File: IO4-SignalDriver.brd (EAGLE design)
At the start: 99.8 x 80.5 mm, 21 parts, among them CON1 CONNECTOR-RJ45-FRONT, IC1 74LS139N, P1 500R, P2 500R, P3 500R, P4 500R, P5 500R, P6 500R

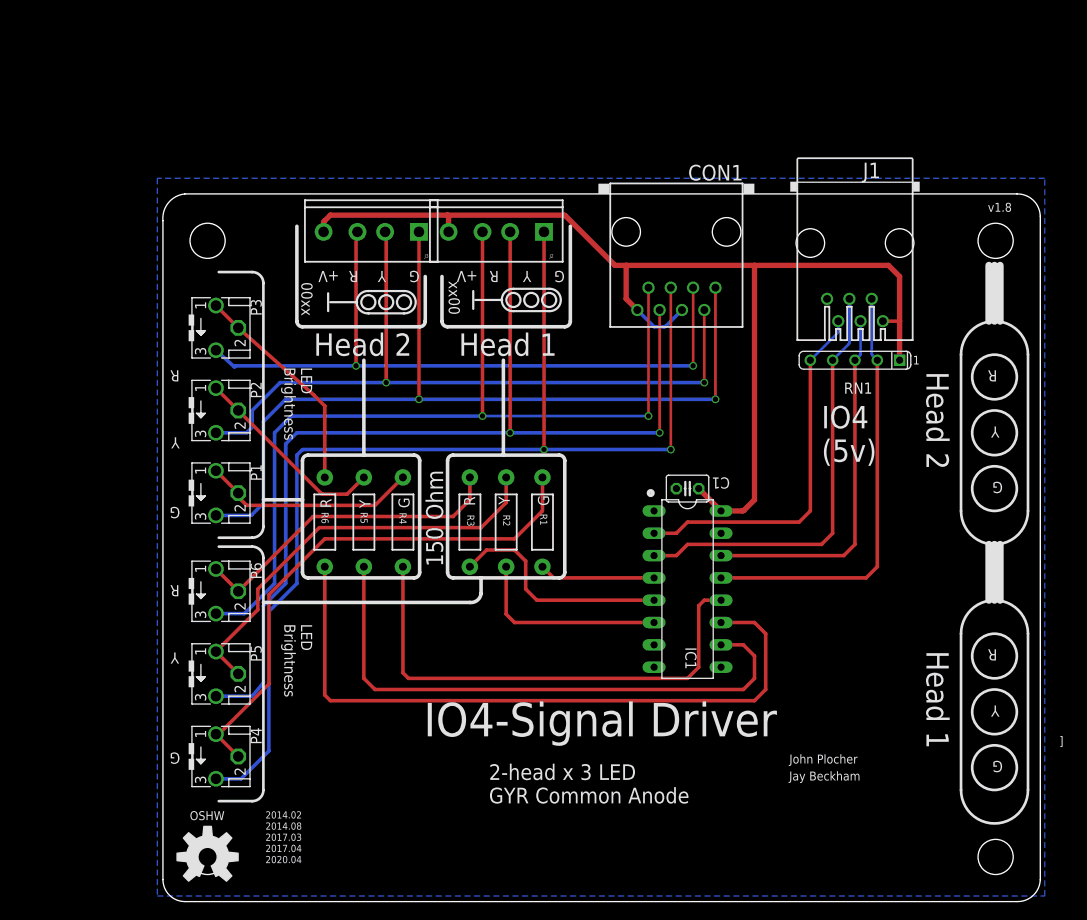
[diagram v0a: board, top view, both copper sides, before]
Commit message: convert to SMT, add 2mmx4 headers
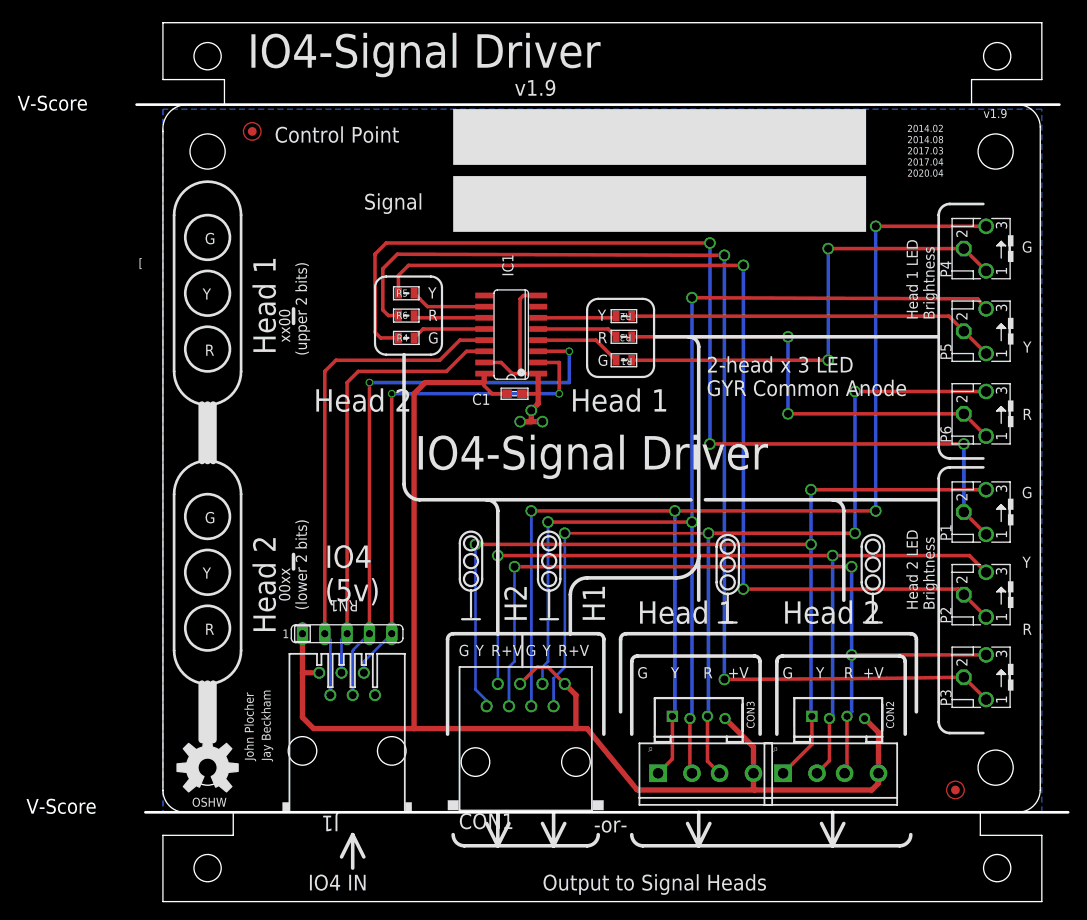
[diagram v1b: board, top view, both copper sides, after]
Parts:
- added CON2, CON3: CONNECTOR-GROVE-4P-2.0-3470130P1, SPCoast:4P-2.0
- added FID1, FID2: FIDUCIAL, SPCoast:FIDUCIAL_1MM
- BOARD1: value (none) -> BOARD80X100
- C1: device rcl:C025-030X050 -> SPCoast:0603-CAP
- CON1: value CONNECTOR-RJ45-FRONT -> (none)
- IC1: value 74LS139N -> 74LS139D; device 74xx-us:DIL16 -> SPCoast:SO16
- J1: device MCP:520250-3 -> SPCoast:RJ25-PANEL
- R1, R2, R3, R4, R5, R6: value 150R -> 470R; device SparkFun:AXIAL-0.4 -> SPCoast:0805-RES
- moved P4 104.4 mm to (93.3, 74.3), turned to 90 degrees
- moved P3 95.6 mm to (93.3, 25.5), turned to 90 degrees
- moved P5 95.3 mm to (93.3, 64.9), turned to 90 degrees
- moved P2 89.5 mm to (93.3, 34.9), turned to 90 degrees
- moved P6 89.3 mm to (93.3, 55.5), turned to 90 degrees
- moved P1 87.0 mm to (93.3, 44.3), turned to 90 degrees
- moved J1 81.7 mm to (21.0, 17.1), turned to 0 degrees
- moved J3 74.4 mm to (70.7, 14.6), turned to 0 degrees
- moved RN1 65.6 mm to (21.0, 30.5), turned to 0 degrees
- moved J2 63.0 mm to (56.5, 14.6), turned to 0 degrees
- moved CON1 62.7 mm to (41.3, 15.9), turned to 0 degrees
- moved IC1 35.2 mm to (39.6, 64.5), turned to 90 degrees
- moved R3 27.4 mm to (52.5, 64.3), turned to 180 degrees
- moved R2 27.0 mm to (52.5, 66.6), turned to 180 degrees
- moved R5 26.5 mm to (27.7, 69.2), turned to 0 degrees
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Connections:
- net G1: now also R4.2; no longer R4.P$2
- net G1-LED: now also CON2.1
- net G1V: now also R4.1; no longer R4.P$1
- net G2: now also R1.2; no longer R1.P$2
- net G2-LED: now also CON3.1
- net G2V: now also R1.1; no longer R1.P$1
- net R1: now also R6.2; no longer R6.P$2
- net R1-LED: now also CON2.3
- net R1V: now also R6.1; no longer R6.P$1
- net R2: now also R3.2; no longer R3.P$2
- net R2-LED: now also CON3.3
- net R2V: now also R3.1; no longer R3.P$1
- net VCC: now also CON2.4, CON3.4
- net Y1: now also R5.2; no longer R5.P$2
- net Y1-LED: now also CON2.2
- net Y1V: now also R5.1; no longer R5.P$1
- net Y2: now also R2.2; no longer R2.P$2
- net Y2-LED: now also CON3.2
- net Y2V: now also R2.1; no longer R2.P$1
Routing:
- net R1V: track 25.0 -> 125.4 mm, vias 0 -> 2
- net G1V: track 24.5 -> 113.5 mm, vias 0 -> 3
- net Y1V: track 22.6 -> 107.5 mm, vias 0 -> 2
- net R1: track 77.5 -> 8.07 mm
- net Y1: track 65.1 -> 8.60 mm
- net G1: track 56.3 -> 8.39 mm
- net VCC: track 130.1 -> 162.8 mm
- net GND: track 0.00 -> 31.1 mm, vias 0 -> 3
- net N$6: track 48.8 -> 66.2 mm, vias 0 -> 2
- net R2: track 26.0 -> 9.22 mm
- net N$5: track 41.7 -> 58.0 mm, vias 0 -> 2
- net R1-LED: track 79.2 -> 93.6 mm, vias 2 -> 3
- net Y2: track 22.6 -> 8.93 mm
- net R2V: track 36.8 -> 50.1 mm, vias 0 -> 2
- net Y1-LED: track 84.6 -> 96.5 mm
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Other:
- board size 99.8 x 80.5 mm -> 106 x 100 mm
- board text added: "-or-"
- board text added: "00xx (lower 2 bits)"
- board text added: "Changes: Silk Screen alignment, tweeking spaced fixed resistors further apart min trace width 16mil SMT components 2mmx4 headers"
- board text added: "Control Point"
- board text added: "H1"
- board text added: "H2"
- board text added: "Head 1 LED Brightness"
- board text added: "Head 2 LED Brightness"
- board text added: "IO4 IN"
- board text added: "Output to Signal Heads"
- board text added: "Signal"
- board text added: "v1.9"
- board text added: "xx00 (upper 2 bits)"
- board text removed: "00xx"
- board text removed: "150 Ohm"
- board text removed: "Changes: Silk Screen alignment, tweeking spaced fixed resistors further apart min trace width 16mil"
- board text removed: "LED Brightness"
- board text removed: "v1.8"
- board text removed: "xx00"

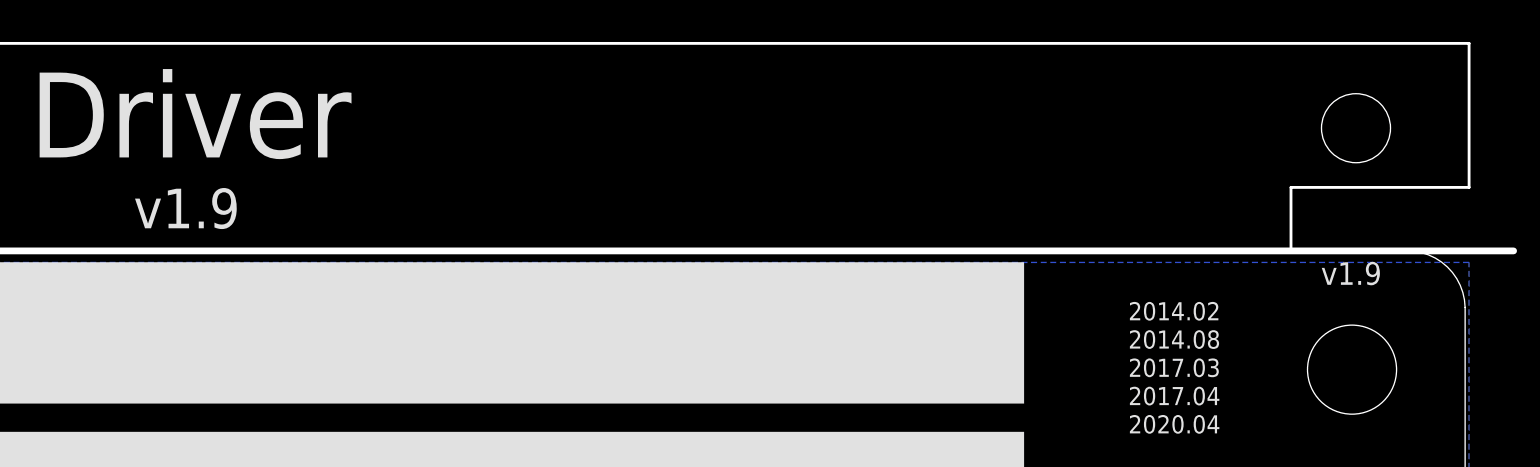
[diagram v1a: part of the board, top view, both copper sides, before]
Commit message: changed silkscreen version info
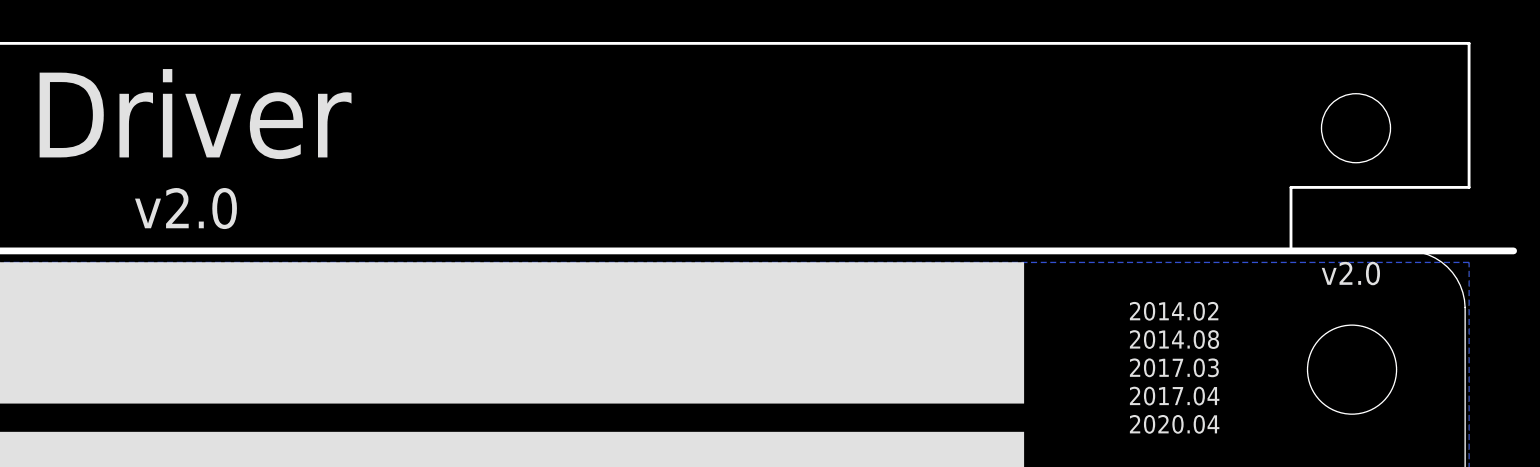
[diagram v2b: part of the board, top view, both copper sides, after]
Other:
- board text added: "v2.0"
- board text removed: "v1.9"
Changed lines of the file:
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@@
 <plain>
 <text x="28.653" y="49.157" size="3.81" layer="21" rot="SR0">IO4-Signal Driver</text>
-<text x="93.345" y="89.154" size="1.016" layer="21" rot="SR0">v1.9</text>
+<text x="93.345" y="89.154" size="1.016" layer="21" rot="SR0">v2.0</text>
 <text x="12.2555" y="16.002" size="1.016" layer="21" rot="SR90">Jay Beckham</text>
 <text x="10.327" y="16.028" size="1.016" layer="21" rot="SR90">John Plocher</text>
@@
 <text x="43.18" y="1.27" size="1.778" layer="21" font="vector" ratio="10">Output to Signal Heads</text>
 <text x="9.603" y="94.877" size="3.81" layer="21" rot="SR0">IO4-Signal Driver</text>
-<text x="40.005" y="91.694" size="1.778" layer="21" rot="SR0">v1.9</text>
+<text x="40.005" y="91.694" size="1.778" layer="21" rot="SR0">v2.0</text>
 <wire x1="38.1" y1="6.35" x2="39.37" y2="8.89" width="0.4064" layer="21"/>
 <wire x1="38.1" y1="6.35" x2="36.83" y2="8.89" width="0.4064" layer="21"/>

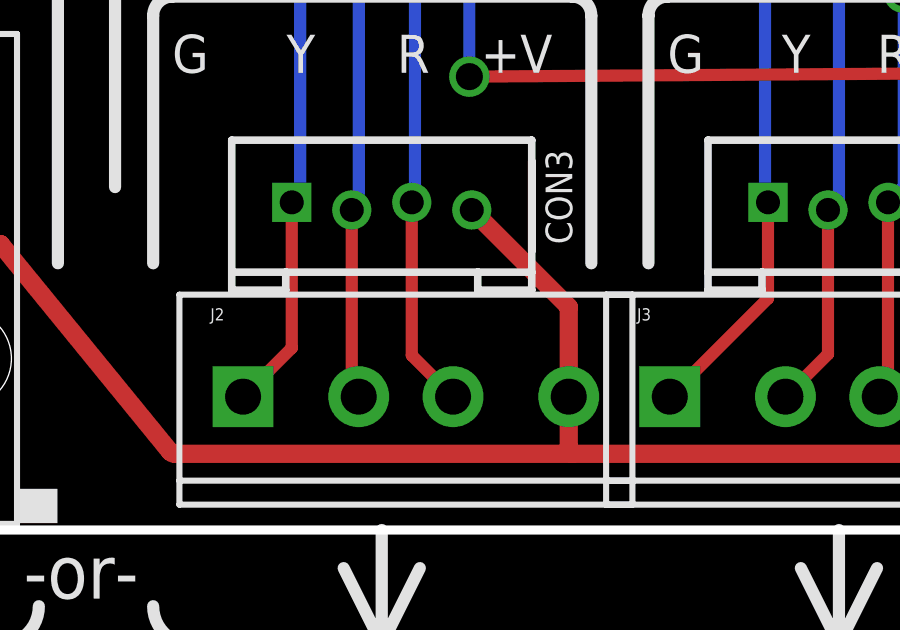
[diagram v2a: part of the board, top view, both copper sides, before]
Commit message: font=vector
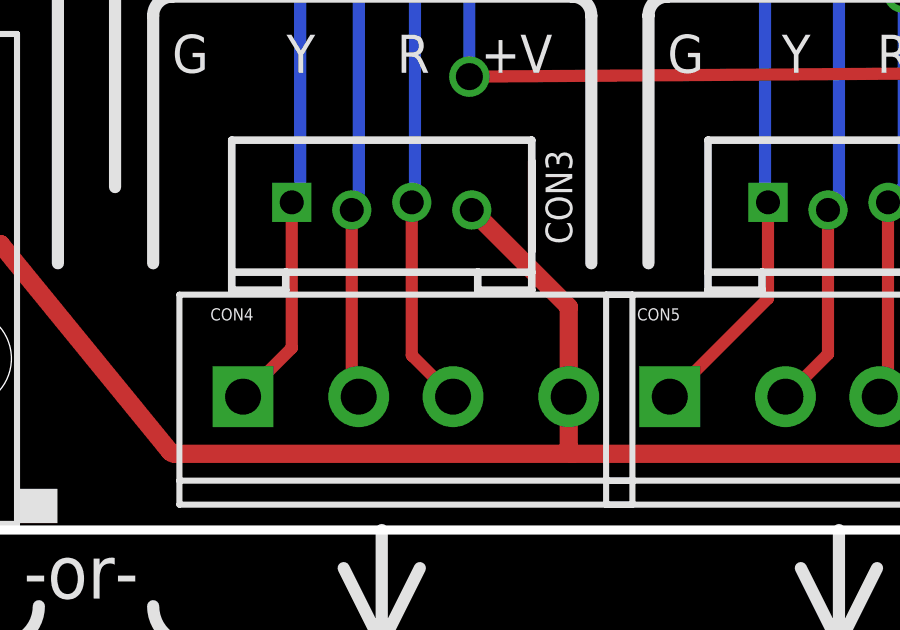
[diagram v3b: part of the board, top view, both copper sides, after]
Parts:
- R1, R2, R3, R4, R5, R6: value 470R -> 330R
- renumbered J2 to CON4, J3 to CON5
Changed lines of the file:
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@@
 <attribute name="VALUE" x="35.179" y="54.737" size="1.27" layer="27" ratio="10" rot="SR0"/>
 </element>
-<element name="R2" library="SPCoast" package="0805-RES" value="470R" x="52.451" y="66.6115" smashed="yes" rot="R180">
+<element name="R2" library="SPCoast" package="0805-RES" value="330R" x="52.451" y="66.6115" smashed="yes" rot="R180">
 <attribute name="NAME" x="53.3" y="66.9685" size="0.8128" layer="25" font="vector" ratio="15" rot="SR180"/>
 </element>
-<element name="R3" library="SPCoast" package="0805-RES" value="470R" x="52.451" y="64.262" smashed="yes" rot="R180">
+<element name="R3" library="SPCoast" package="0805-RES" value="330R" x="52.451" y="64.262" smashed="yes" rot="R180">
 <attribute name="NAME" x="53.292" y="64.565" size="0.8128" layer="25" font="vector" ratio="15" rot="SR180"/>
 </element>
-<element name="R1" library="SPCoast" package="0805-RES" value="470R" x="52.451" y="61.595" smashed="yes" rot="R180">
+<element name="R1" library="SPCoast" package="0805-RES" value="330R" x="52.451" y="61.595" smashed="yes" rot="R180">
 <attribute name="NAME" x="53.4" y="61.852" size="0.8128" layer="25" font="vector" ratio="15" rot="SR180"/>
 </element>
-<element name="R5" library="SPCoast" package="0805-RES" value="470R" x="27.686" y="69.215" smashed="yes">
+<element name="R5" library="SPCoast" package="0805-RES" value="330R" x="27.686" y="69.215" smashed="yes">
 <attribute name="NAME" x="26.543" y="68.834" size="0.8128" layer="25" font="vector" ratio="15" rot="SR0"/>
 </element>
-<element name="R6" library="SPCoast" package="0805-RES" value="470R" x="27.686" y="66.675" smashed="yes">
+<element name="R6" library="SPCoast" package="0805-RES" value="330R" x="27.686" y="66.675" smashed="yes">
 <attribute name="NAME" x="26.543" y="66.294" size="0.8128" layer="25" font="vector" ratio="15" rot="SR0"/>
 </element>
-<element name="R4" library="SPCoast" package="0805-RES" value="470R" x="27.686" y="64.135" smashed="yes">
+<element name="R4" library="SPCoast" package="0805-RES" value="330R" x="27.686" y="64.135" smashed="yes">
 <attribute name="NAME" x="26.589" y="63.732" size="0.8128" layer="25" font="vector" ratio="15" rot="SR0"/>
 </element>
-<element name="J2" library="SparkFun" package="SCREWTERMINAL-3.5MM-4_LOCK" value="" x="56.515" y="14.605"/>
-<element name="J3" library="SparkFun" package="SCREWTERMINAL-3.5MM-4_LOCK" value="" x="70.739" y="14.605"/>
+<element name="CON4" library="SparkFun" package="SCREWTERMINAL-3.5MM-4_LOCK" value="" x="56.515" y="14.605"/>
+<element name="CON5" library="SparkFun" package="SCREWTERMINAL-3.5MM-4_LOCK" value="" x="70.739" y="14.605"/>
 <element name="RN1" library="resistor-sil" package="SIL5" value="4k7" x="20.955" y="30.48" smashed="yes">
 <attribute name="MF" value="" x="20.955" y="30.48" size="1.778" layer="27" display="off"/>
@@
 <contactref element="IC1" pad="16"/>
 <contactref element="C1" pad="1"/>
-<contactref element="J2" pad="4"/>
-<contactref element="J3" pad="4"/>
+<contactref element="CON4" pad="4"/>
+<contactref element="CON5" pad="4"/>
 <contactref element="RN1" pad="1"/>
 <contactref element="J1" pad="1"/>
@@
 </signal>
 <signal name="G1-LED">
-<contactref element="J3" pad="1"/>
+<contactref element="CON5" pad="1"/>
 <contactref element="P1" pad="CW"/>
 <contactref element="CON1" pad="1"/>
@@
 </signal>
 <signal name="R1-LED">
-<contactref element="J3" pad="3"/>
+<contactref element="CON5" pad="3"/>
 <contactref element="P3" pad="CW"/>
 <contactref element="CON1" pad="3"/>
@@
 </signal>
 <signal name="Y1-LED">
-<contactref element="J3" pad="2"/>
+<contactref element="CON5" pad="2"/>
 <contactref element="P2" pad="CW"/>
 <contactref element="CON1" pad="2"/>
@@
 </signal>
 <signal name="G2-LED">
-<contactref element="J2" pad="1"/>
+<contactref element="CON4" pad="1"/>
 <contactref element="P4" pad="CW"/>
 <contactref element="CON1" pad="5"/>
@@
 </signal>
 <signal name="R2-LED">
-<contactref element="J2" pad="3"/>
+<contactref element="CON4" pad="3"/>
 <contactref element="P6" pad="CW"/>
 <contactref element="CON1" pad="7"/>
@@
 </signal>
 <signal name="Y2-LED">
-<contactref element="J2" pad="2"/>
+<contactref element="CON4" pad="2"/>
 <contactref element="P5" pad="CW"/>
 <contactref element="CON1" pad="6"/>
